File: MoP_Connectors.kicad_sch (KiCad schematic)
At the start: 0 parts

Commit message: added SPI and I2C hierarchical connectors to sensors sheet and reordered page numbers
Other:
- company: (none) -> ESE - Conestoga
- title: (none) -> MoP - Connectors
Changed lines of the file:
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@@
 	(generator_version "8.0")
 	(paper "A4")
+	(title_block
+		(title "MoP - Connectors")
+		(rev "0")
+		(company "ESE - Conestoga")
+		(comment 1 "Nigel Sinclair")
+	)
 )

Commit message: changed ref designators to be consistent accross sheets
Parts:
- added J22: Conn_02x22_Top_Bottom, symbol Connector_Generic:Conn_02x22_Top_Bottom
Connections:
- new net ENC.L: J22.7 (Pin_7)
- new net ENC.R: J22.8 (Pin_8)
- new net GND: J22.23 (Pin_23), J22.24 (Pin_24), J22.25 (Pin_25), J22.26 (Pin_26), J22.27 (Pin_27), J22.28 (Pin_28), J22.29 (Pin_29), J22.30 (Pin_30), J22.31 (Pin_31), J22.32 (Pin_32), J22.33 (Pin_33), J22.34 (Pin_34), J22.35 (Pin_35), J22.36 (Pin_36), J22.37 (Pin_37), J22.38 (Pin_38), J22.39 (Pin_39), J22.40 (Pin_40), J22.41 (Pin_41), J22.42 (Pin_42), J22.43 (Pin_43), J22.44 (Pin_44)
- new net LCD.D4: J22.3 (Pin_3)
- new net LCD.D5: J22.4 (Pin_4)
- new net LCD.D6: J22.5 (Pin_5)
- new net LCD.D7: J22.6 (Pin_6)
- new net LCD.EN: J22.2 (Pin_2)
- new net LCD.RS: J22.1 (Pin_1)
- new net LDCM.1: J22.14 (Pin_14)
- new net LDCM.2: J22.15 (Pin_15)
- new net LDCM.EN: J22.16 (Pin_16)
- new net LMT.L: J22.9 (Pin_9)
- new net LMT.R: J22.10 (Pin_10)
- new net RDCM.1: J22.11 (Pin_11)
- new net RDCM.2: J22.12 (Pin_12)
- new net RDCM.EN: J22.13 (Pin_13)
- new net Servo.Camera: J22.17 (Pin_17)
- new net Servo.Steering: J22.18 (Pin_18)
- new net Stepper0: J22.19 (Pin_19)
- new net Stepper1: J22.20 (Pin_20)
- new net Stepper2: J22.21 (Pin_21)
- new net Stepper3: J22.22 (Pin_22)
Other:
- note added: "Debug Connector"
- title: MoP - Connectors -> MoP - Debug

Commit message: Finished schematics
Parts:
- added J1102: PWR_02x20, Connector_PinHeader_2.54mm:PinHeader_2x20_P2.54mm_Vertical, symbol Connector_Generic:Conn_02x20_Counter_Clockwise
- added J1103: COMMS_02x20, Connector_PinHeader_2.54mm:PinHeader_2x20_P2.54mm_Vertical, symbol Connector_Generic:Conn_02x20_Counter_Clockwise
- J1101: renamed from J22; value Conn_02x22_Top_Bottom -> Debug_02x22; footprint (none) -> Connector_PinHeader_1.00mm:PinHeader_2x19_P1.00mm_Vertical
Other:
- note added: "Stackup Connectors"
- moved on the sheet: J1101

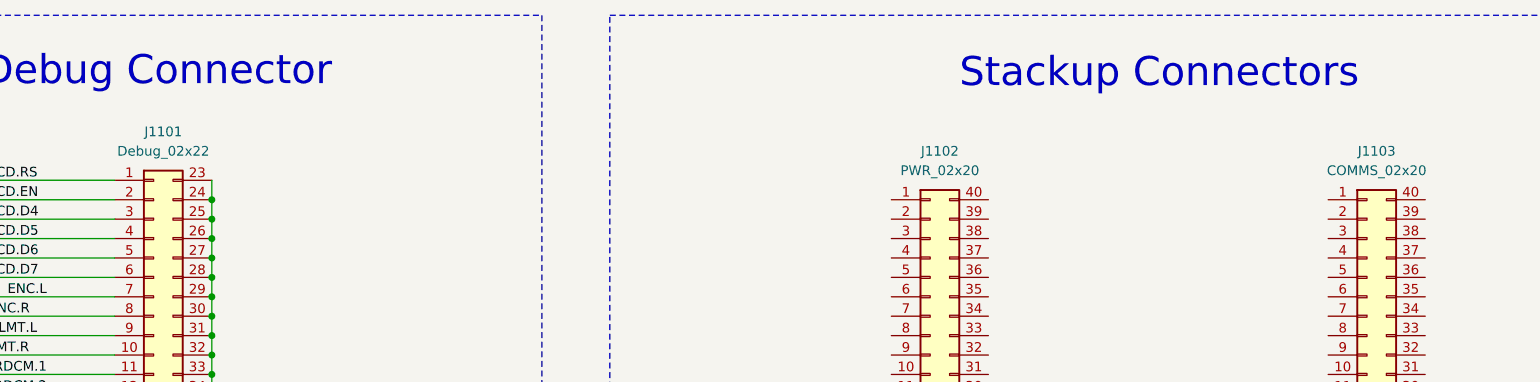
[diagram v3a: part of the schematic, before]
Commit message: Added subproject for EPS PCB
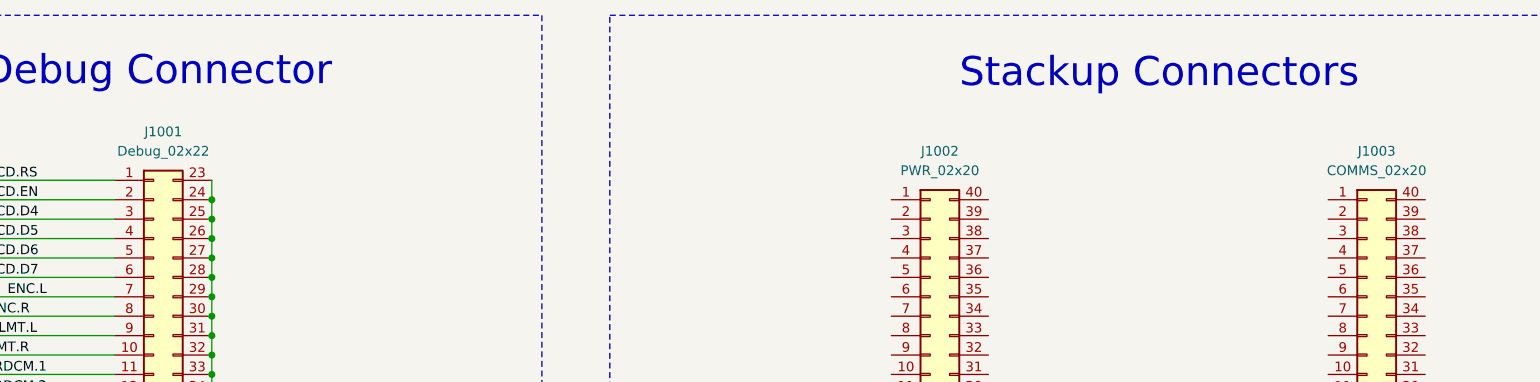
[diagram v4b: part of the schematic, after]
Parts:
- renumbered J1101 to J1001, J1102 to J1002, J1103 to J1003
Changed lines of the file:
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@@
 		(dnp no)
 		(fields_autoplaced yes)
-		(property "Reference" "J1102"
+		(property "Reference" "J1002"
 			(at 179.07 38.1 0)
 			(effects
@@
 		)
 		(property "Description" "Generic connector, double row, 02x20, counter clockwise pin numbering scheme (similar to DIP package numbering), script generated (kicad-library-utils/schlib/autogen/connector/)"
+			(at 177.8 67.31 0)
+			(effects
+				(font
+					(size 1.27 1.27)
+				)
+				(hide yes)
+			)
+		)
+		(property "DigiKey#" ""
+			(at 177.8 67.31 0)
+			(effects
+				(font
+					(size 1.27 1.27)
+				)
+				(hide yes)
+			)
+		)
+		(property "P#" ""
+			(at 177.8 67.31 0)
+			(effects
+				(font
+					(size 1.27 1.27)
+				)
+				(hide yes)
+			)
+		)
+		(property "SNAPEDA_PN" ""
+			(at 177.8 67.31 0)
+			(effects
+				(font
+					(size 1.27 1.27)
+				)
+				(hide yes)
+			)
+		)
+		(property "Sim.Device" ""
+			(at 177.8 67.31 0)
+			(effects
+				(font
+					(size 1.27 1.27)
+				)
+				(hide yes)
+			)
+		)
+		(property "Sim.Pins" ""
+			(at 177.8 67.31 0)
+			(effects
+				(font
+					(size 1.27 1.27)
+				)
+				(hide yes)
+			)
+		)
+		(property "Sim.Type" ""
 			(at 177.8 67.31 0)
 			(effects
@@
 			(project ""
 				(path "/4d76798e-9a11-4d8d-a723-72f274a89091/66fadfde-b926-4c46-9708-f37e1f1905e9"
-					(reference "J1102")
+					(reference "J1002")
 					(unit 1)
 				)
@@
 		(dnp no)
 		(fields_autoplaced yes)
-		(property "Reference" "J1103"
+		(property "Reference" "J1003"
 			(at 236.22 38.1 0)
 			(effects
@@
 		)
 		(property "Description" "Generic connector, double row, 02x20, counter clockwise pin numbering scheme (similar to DIP package numbering), script generated (kicad-library-utils/schlib/autogen/connector/)"
+			(at 234.95 67.31 0)
+			(effects
+				(font
+					(size 1.27 1.27)
+				)
+				(hide yes)
+			)
+		)
+		(property "DigiKey#" ""
+			(at 234.95 67.31 0)
+			(effects
+				(font
+					(size 1.27 1.27)
+				)
+				(hide yes)
+			)
+		)
+		(property "P#" ""
+			(at 234.95 67.31 0)
+			(effects
+				(font
+					(size 1.27 1.27)
+				)
+				(hide yes)
+			)
+		)
+		(property "SNAPEDA_PN" ""
+			(at 234.95 67.31 0)
+			(effects
+				(font
+					(size 1.27 1.27)
+				)
+				(hide yes)
+			)
+		)
+		(property "Sim.Device" ""
+			(at 234.95 67.31 0)
+			(effects
+				(font
+					(size 1.27 1.27)
+				)
+				(hide yes)
+			)
+		)
+		(property "Sim.Pins" ""
+			(at 234.95 67.31 0)
+			(effects
+				(font
+					(size 1.27 1.27)
+				)
+				(hide yes)
+			)
+		)
+		(property "Sim.Type" ""
 			(at 234.95 67.31 0)
 			(effects
@@
 			(project "MoP"
 				(path "/4d76798e-9a11-4d8d-a723-72f274a89091/66fadfde-b926-4c46-9708-f37e1f1905e9"
-					(reference "J1103")
+					(reference "J1003")
 					(unit 1)
 				)
@@
 		(dnp no)
 		(fields_autoplaced yes)
-		(property "Reference" "J1101"
+		(property "Reference" "J1001"
 			(at 77.47 35.56 0)
 			(effects
@@
 		)
 		(property "Description" "Generic connector, double row, 02x22, top/bottom pin numbering scheme (row 1: 1...pins_per_row, row2: pins_per_row+1 ... num_pins), script generated (kicad-library-utils/schlib/autogen/connector/)"
+			(at 76.2 67.31 0)
+			(effects
+				(font
+					(size 1.27 1.27)
+				)
+				(hide yes)
+			)
+		)
+		(property "DigiKey#" ""
+			(at 76.2 67.31 0)
+			(effects
+				(font
+					(size 1.27 1.27)
+				)
+				(hide yes)
+			)
+		)
+		(property "P#" ""
+			(at 76.2 67.31 0)
+			(effects
+				(font
+					(size 1.27 1.27)
+				)
+				(hide yes)
+			)
+		)
+		(property "SNAPEDA_PN" ""
+			(at 76.2 67.31 0)
+			(effects
+				(font
+					(size 1.27 1.27)
+				)
+				(hide yes)
+			)
+		)
+		(property "Sim.Device" ""
+			(at 76.2 67.31 0)
+			(effects
+				(font
+					(size 1.27 1.27)
+				)
+				(hide yes)
+			)
+		)
+		(property "Sim.Pins" ""
+			(at 76.2 67.31 0)
+			(effects
+				(font
+					(size 1.27 1.27)
+				)
+				(hide yes)
+			)
+		)
+		(property "Sim.Type" ""
 			(at 76.2 67.31 0)
 			(effects
@@
 			(project ""
 				(path "/4d76798e-9a11-4d8d-a723-72f274a89091/66fadfde-b926-4c46-9708-f37e1f1905e9"
-					(reference "J1101")
+					(reference "J1001")
 					(unit 1)
 				)

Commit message: added OBC
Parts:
- removed J1001: Debug_02x22, Connector_PinHeader_1.00mm:PinHeader_2x19_P1.00mm_Vertical, symbol Connector_Generic:Conn_02x22_Top_Bottom
- removed J1002: PWR_02x20, Connector_PinHeader_2.54mm:PinHeader_2x20_P2.54mm_Vertical, symbol Connector_Generic:Conn_02x20_Counter_Clockwise
- removed J1003: COMMS_02x20, Connector_PinHeader_2.54mm:PinHeader_2x20_P2.54mm_Vertical, symbol Connector_Generic:Conn_02x20_Counter_Clockwise
- added J701: Conn_01x22, Connector_PinHeader_2.54mm:PinHeader_1x22_P2.54mm_Vertical, symbol Connector_Generic:Conn_01x22
- added J702: Conn_02x20_Counter_Clockwise, Nigels_Library:PinHeader_2x20_P2.54mm_Vertical_CC, symbol Connector_Generic:Conn_02x20_Counter_Clockwise
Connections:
- net ENC.L: now also J701.7 (Pin_7)
- net ENC.R: now also J701.8 (Pin_8)
- net GND: now also J702.1 (Pin_1), J702.37 (Pin_37), J702.4 (Pin_4), J702.40 (Pin_40)
- net LCD.D4: now also J701.3 (Pin_3)
- net LCD.D5: now also J701.4 (Pin_4)
- net LCD.D6: now also J701.5 (Pin_5)
- net LCD.D7: now also J701.6 (Pin_6)
- net LCD.EN: now also J701.2 (Pin_2)
- net LCD.RS: now also J701.1 (Pin_1)
- net LDCM.1: now also J701.14 (Pin_14), J702.10 (Pin_10)
- net LDCM.2: now also J701.15 (Pin_15), J702.11 (Pin_11)
- net LDCM.EN: now also J701.16 (Pin_16), J702.14 (Pin_14)
- net LMT.L: now also J701.9 (Pin_9)
- net LMT.R: now also J701.10 (Pin_10)
- net RDCM.1: now also J701.11 (Pin_11), J702.12 (Pin_12)
- net RDCM.2: now also J701.12 (Pin_12), J702.13 (Pin_13)
- net RDCM.EN: now also J701.13 (Pin_13), J702.15 (Pin_15)
- net Servo.Camera: now also J701.17 (Pin_17), J702.5 (Pin_5)
- net Servo.Steering: now also J701.18 (Pin_18), J702.6 (Pin_6)
- net Stepper0: now also J701.19 (Pin_19), J702.34 (Pin_34)
- net Stepper1: now also J701.20 (Pin_20), J702.33 (Pin_33)
- net Stepper2: now also J701.21 (Pin_21), J702.32 (Pin_32)
- net Stepper3: now also J701.22 (Pin_22), J702.31 (Pin_31)
- new net GPIO0: J702.7 (Pin_7)
- new net GPIO1: J702.8 (Pin_8)
- new net GPIO2: J702.9 (Pin_9)
- new net GPIO3: J702.16 (Pin_16)
- new net GPIO4: J702.17 (Pin_17)
- new net GPIO5: J702.18 (Pin_18)
- new net GPIO6: J702.19 (Pin_19)
- new net GPIO7: J702.20 (Pin_20)
- new net GPIO8: J702.22 (Pin_22)
- new net GPIO9: J702.21 (Pin_21)
- new net Keypad0: J702.30 (Pin_30)
- new net Keypad1: J702.29 (Pin_29)
- new net Keypad2: J702.28 (Pin_28)
- new net Keypad3: J702.27 (Pin_27)
- new net Keypad4: J702.26 (Pin_26)
- new net Keypad5: J702.25 (Pin_25)
- new net Keypad6: J702.24 (Pin_24)
- new net Keypad7: J702.23 (Pin_23)
- new net R3V3: J702.3 (Pin_3), J702.38 (Pin_38)
- new net R5V: J702.2 (Pin_2), J702.39 (Pin_39)
- no-connect marks 0 -> 2
